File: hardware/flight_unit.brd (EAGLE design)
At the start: 160 x 100 mm, 25 parts, among them IC2 7805T, J1 DCJ0202, J2 CONN_20X2SHROUDED, T1 THERMISTOR-2,5, U1 4MB Flash, U2 4MB Flash, U3 4MB Flash

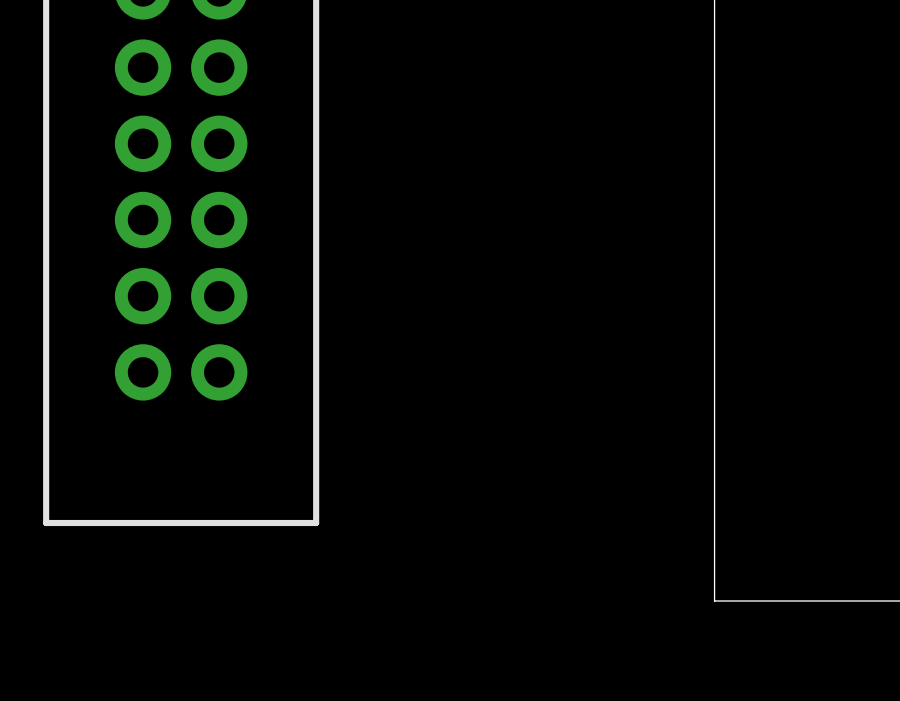
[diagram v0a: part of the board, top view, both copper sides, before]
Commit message: updated i/o headers
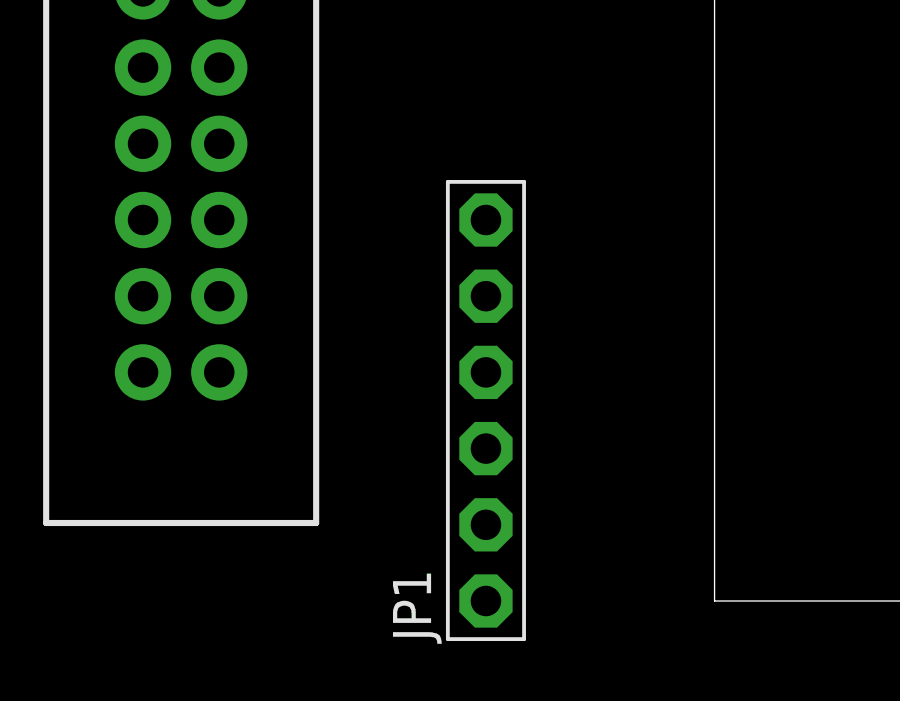
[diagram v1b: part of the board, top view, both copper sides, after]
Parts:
- added JP1: (no value), adafruit:1X06-BIG
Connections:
- removed net D_0: U$1.0/RX
- removed net D_1: U$1.1/TX
- removed net D_2: U$1.2
- removed net D_3: U$1.3/CANTX
- removed net D_4: U$1.4/CANRX
- new net SC_D0: J2.8, U$1.0/RX
- new net SC_D1: J2.12, U$1.1/TX
- new net SC_D2: J2.16, U$1.2
- new net SC_D3: J2.22, U$1.3/CANTX
- new net SC_D4: J2.36, U$1.4/CANRX
- net +3V3: now also U$3.VIN
- net GND: now also JP1.5, JP1.6, U$3.GND
- net IIC_SCL: now also J2.29, U$3.SCL
- net IIC_SDA: now also J2.7, U$3.SDA
- net SC_A0: now also JP1.1
- net SC_A1: now also JP1.2
- net SC_A2: now also JP1.3
- net SC_A3: now also JP1.4
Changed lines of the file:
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@@
 </element>
 <element name="U$3" library="adafruit" package="BNO055_BREAKOUT" value="IMU_BREAKOUT" x="10.16" y="64.77" smashed="yes"/>
+<element name="JP1" library="adafruit" package="1X06-BIG" value="" x="-7.62" y="6.35" smashed="yes" rot="R90">
+<attribute name="NAME" x="-9.4488" y="-1.3462" size="1.27" layer="25" ratio="10" rot="R90"/>
+<attribute name="VALUE" x="-4.445" y="-1.27" size="1.27" layer="27" rot="R90"/>
+</element>
 </elements>
 <signals>
@@
 <contactref element="T1" pad="1"/>
 <contactref element="R8" pad="1"/>
+<contactref element="U$3" pad="VIN"/>
 <wire x1="-20.19" y1="104.14" x2="-13.84" y2="104.14" width="0" layer="19" extent="1-1"/>
 <wire x1="-26.54" y1="104.14" x2="-20.19" y2="104.14" width="0" layer="19" extent="1-1"/>
@@
 <wire x1="-74.295" y1="106.94" x2="-68.58" y2="110.49" width="0" layer="19" extent="1-1"/>
 <wire x1="-48.26" y1="80.01" x2="-56.515" y2="106.94" width="0" layer="19" extent="1-1"/>
+<wire x1="17.145" y1="66.04" x2="-13.84" y2="104.14" width="0" layer="19" extent="1-1"/>
 <wire x1="-57.15" y1="2.54" x2="-48.26" y2="80.01" width="0" layer="19" extent="1-1"/>
 </signal>
@@
 <contactref element="RN2" pad="7"/>
 <contactref element="RN2" pad="5"/>
+<contactref element="U$3" pad="GND"/>
+<contactref element="JP1" pad="6"/>
+<contactref element="JP1" pad="5"/>
 <wire x1="-41.91" y1="118.11" x2="-31.75" y2="118.11" width="0" layer="19" extent="1-1"/>
 <wire x1="-52.07" y1="118.11" x2="-41.91" y2="118.11" width="0" layer="19" extent="1-1"/>
@@
 <wire x1="-16.51" y1="15.24" x2="-16.51" y2="20.32" width="0" layer="19" extent="1-1"/>
 <wire x1="-19.05" y1="7.62" x2="-16.51" y2="15.24" width="0" layer="19" extent="1-1"/>
+<wire x1="-7.62" y1="12.7" x2="-16.51" y2="15.24" width="0" layer="19" extent="1-1"/>
+<wire x1="-7.62" y1="10.16" x2="-7.62" y2="12.7" width="0" layer="19" extent="1-1"/>
 <wire x1="-34.415" y1="7.62" x2="-19.05" y2="7.62" width="0" layer="19" extent="1-1"/>
 <wire x1="-34.415" y1="5.08" x2="-34.415" y2="7.62" width="0" layer="19" extent="1-1"/>
@@
 <wire x1="-48.385" y1="10.16" x2="-48.385" y2="5.08" width="0" layer="19" extent="1-1"/>
 <wire x1="-59.69" y1="2.54" x2="-48.385" y2="5.08" width="0" layer="19" extent="1-1"/>
+<wire x1="22.225" y1="66.04" x2="-16.51" y2="50.8" width="0" layer="19" extent="1-1"/>
 </signal>
 <signal name="SC_5V0">
@@
 <signal name="IIC_SDA">
 <contactref element="U$1" pad="18/A4/SDA"/>
+<contactref element="U$3" pad="SDA"/>
+<contactref element="J2" pad="7"/>
+<wire x1="-19.05" y1="48.26" x2="24.765" y2="66.04" width="0" layer="19" extent="1-1"/>
+<wire x1="-27.94" y1="80.01" x2="-19.05" y2="48.26" width="0" layer="19" extent="1-1"/>
 </signal>
 <signal name="IIC_SCL">
 <contactref element="U$1" pad="19/A5/SCL"/>
-</signal>
-<signal name="D_0">
-<contactref element="U$1" pad="0/RX"/>
-</signal>
-<signal name="D_1">
-<contactref element="U$1" pad="1/TX"/>
-</signal>
-<signal name="D_2">
-<contactref element="U$1" pad="2"/>
-</signal>
-<signal name="D_3">
-<contactref element="U$1" pad="3/CANTX"/>
-</signal>
-<signal name="D_4">
-<contactref element="U$1" pad="4/CANRX"/>
+<contactref element="U$3" pad="SCL"/>
+<contactref element="J2" pad="29"/>
+<wire x1="-30.48" y1="80.01" x2="27.305" y2="66.04" width="0" layer="19" extent="1-1"/>
+<wire x1="-19.05" y1="20.32" x2="-30.48" y2="80.01" width="0" layer="19" extent="1-1"/>
 </signal>
 <signal name="LED_0">
@@
 <signal name="SC_A3">
 <contactref element="RN2" pad="13"/>
+<contactref element="JP1" pad="4"/>
+<wire x1="-7.62" y1="7.62" x2="-40.515" y2="12.7" width="0" layer="19" extent="1-1"/>
 </signal>
 <signal name="SC_A2">
 <contactref element="RN2" pad="14"/>
+<contactref element="JP1" pad="3"/>
+<wire x1="-7.62" y1="5.08" x2="-40.515" y2="15.24" width="0" layer="19" extent="1-1"/>
 </signal>
 <signal name="SC_A1">
 <contactref element="RN2" pad="15"/>
+<contactref element="JP1" pad="2"/>
+<wire x1="-7.62" y1="2.54" x2="-40.515" y2="17.78" width="0" layer="19" extent="1-1"/>
 </signal>
 <signal name="SC_A0">
 <contactref element="RN2" pad="16"/>
+<contactref element="JP1" pad="1"/>
+<wire x1="-7.62" y1="0" x2="-40.515" y2="20.32" width="0" layer="19" extent="1-1"/>
+</signal>
+<signal name="SC_D0">
+<contactref element="J2" pad="8"/>
+<contactref element="U$1" pad="0/RX"/>
+<wire x1="-45.72" y1="64.77" x2="-16.51" y2="48.26" width="0" layer="19" extent="1-1"/>
+</signal>
+<signal name="SC_D1">
+<contactref element="J2" pad="12"/>
+<contactref element="U$1" pad="1/TX"/>
+<wire x1="-43.18" y1="64.77" x2="-16.51" y2="43.18" width="0" layer="19" extent="1-1"/>
+</signal>
+<signal name="SC_D2">
+<contactref element="J2" pad="16"/>
+<contactref element="U$1" pad="2"/>
+<wire x1="-40.64" y1="64.77" x2="-16.51" y2="38.1" width="0" layer="19" extent="1-1"/>
+</signal>
+<signal name="SC_D3">
+<contactref element="J2" pad="22"/>
+<contactref element="U$1" pad="3/CANTX"/>
+<wire x1="-16.51" y1="30.48" x2="-38.1" y2="64.77" width="0" layer="19" extent="1-1"/>
+</signal>
+<signal name="SC_D4">
+<contactref element="J2" pad="36"/>
+<contactref element="U$1" pad="4/CANRX"/>
+<wire x1="-16.51" y1="12.7" x2="-35.56" y2="64.77" width="0" layer="19" extent="1-1"/>
 </signal>
 </signals>

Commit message: added start of fram framework
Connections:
- net MEM_CS0: now also U$1.8; no longer U$1.10/CS
- net MEM_CS2: now also U$1.10/CS; no longer U$1.8
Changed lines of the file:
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@@
 </signal>
 <signal name="MEM_CS0">
-<contactref element="U$1" pad="10/CS"/>
 <contactref element="U1" pad="1"/>
-<wire x1="-56.515" y1="101.34" x2="-20.32" y2="64.77" width="0" layer="19" extent="1-1"/>
+<contactref element="U$1" pad="8"/>
+<wire x1="-25.4" y1="64.77" x2="-56.515" y2="101.34" width="0" layer="19" extent="1-1"/>
 </signal>
 <signal name="MEM_CS1">
@@
 </signal>
 <signal name="MEM_CS2">
-<contactref element="U$1" pad="8"/>
 <contactref element="U3" pad="1"/>
-<wire x1="-74.295" y1="101.34" x2="-25.4" y2="64.77" width="0" layer="19" extent="1-1"/>
+<contactref element="U$1" pad="10/CS"/>
+<wire x1="-74.295" y1="101.34" x2="-20.32" y2="64.77" width="0" layer="19" extent="1-1"/>
 </signal>
 <signal name="IIC_SDA">

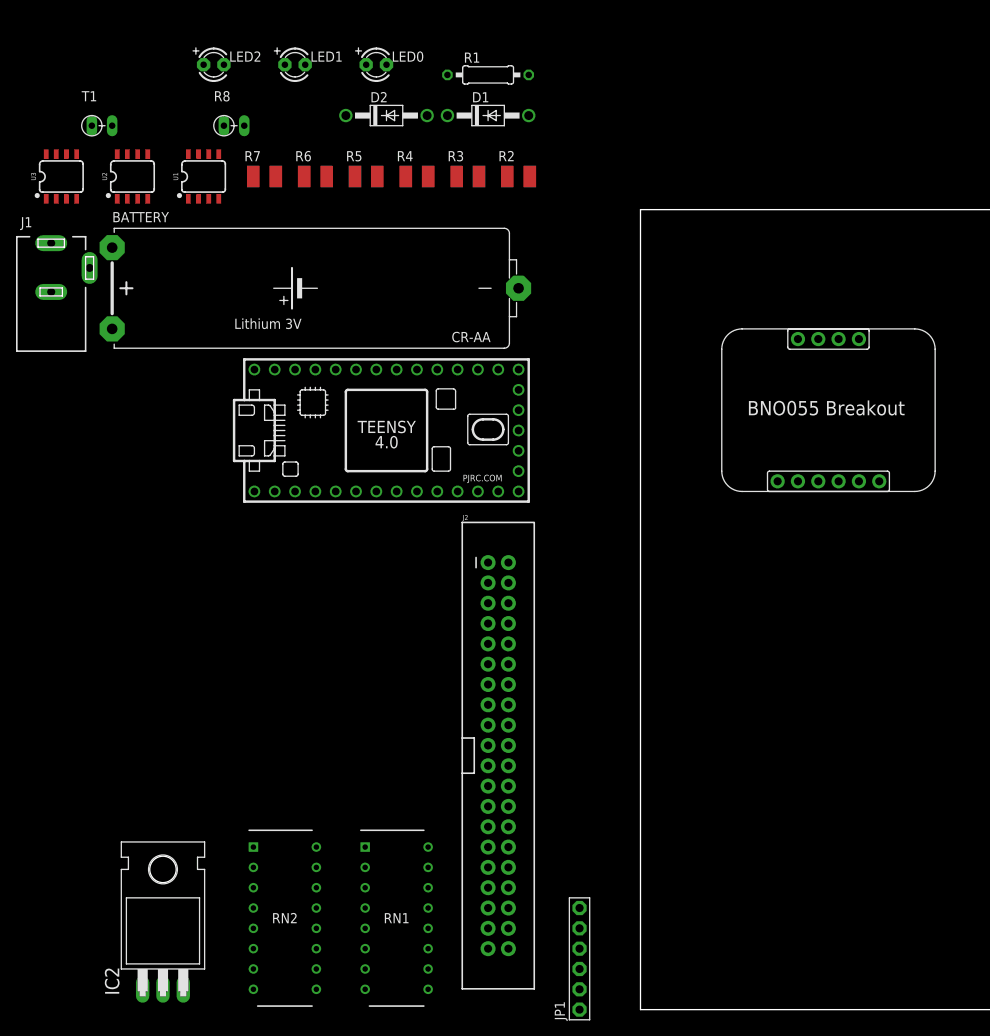
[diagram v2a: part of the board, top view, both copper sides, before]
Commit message: fix back annotation error
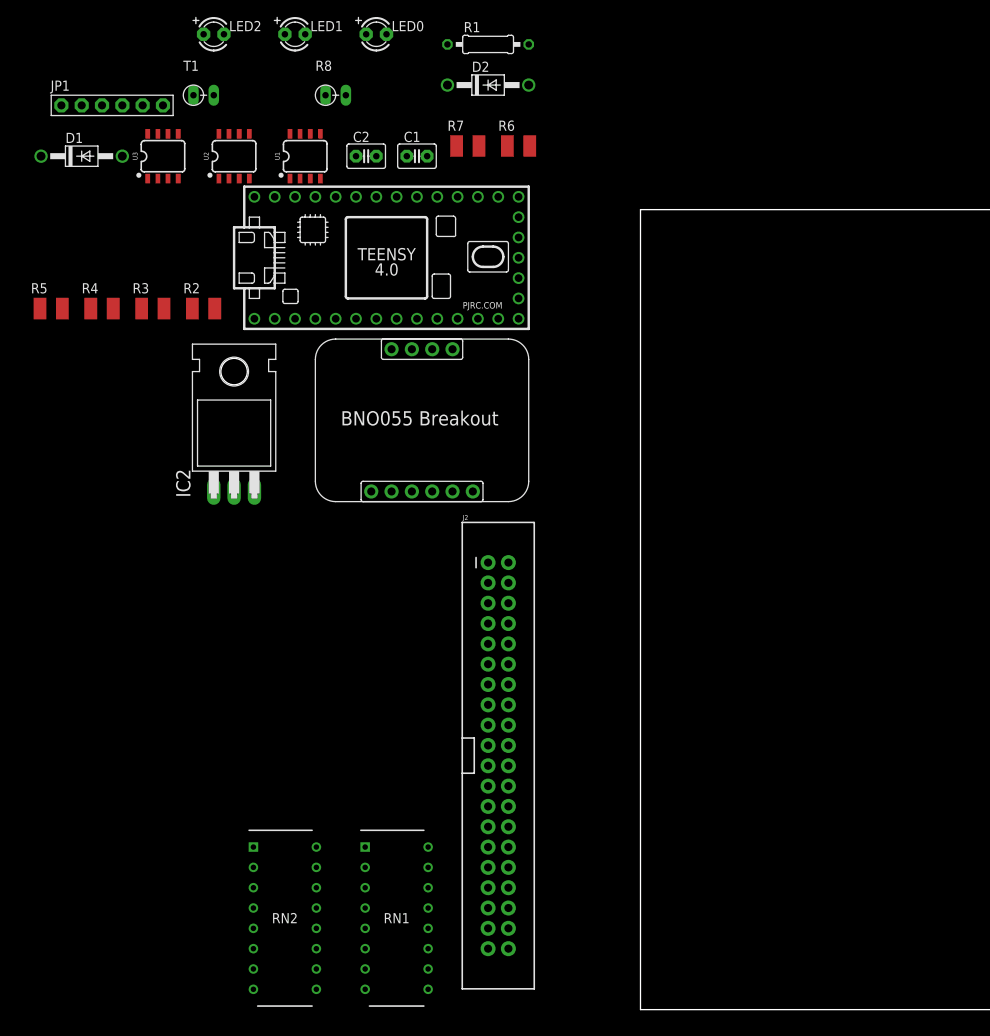
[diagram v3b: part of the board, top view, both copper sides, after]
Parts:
- removed BATTERY: 5V, battery:CRAA
- removed J1: DCJ0202, con-jack:DCJ0202
- added C1, C2: 0.1uf, capacitor-wima:C2.5-3
- R1: value 1k -> 3.3k
- moved JP1 121.6 mm to (-66.0, 113.0), turned to 0 degrees
- moved IC2 62.9 mm to (-50.8, 74.9)
- moved D1 51.1 mm to (-69.8, 106.7)
- moved U$3 50.8 mm to (-40.6, 63.5)
- moved R3 42.7 mm to (-61.0, 87.6)
- moved R4 42.7 mm to (-67.3, 87.6)
- moved R2 42.7 mm to (-54.6, 87.6)
- moved R5 42.7 mm to (-73.7, 87.6)
- moved R7 25.7 mm to (-21.6, 108.0)
- moved R6 25.7 mm to (-15.2, 108.0)
- moved U$1 21.6 mm to (-31.8, 94.0)
- moved T1 13.3 mm to (-54.6, 114.3)
- moved D2 13.3 mm to (-19.1, 115.6)
- moved R8 13.3 mm to (-38.1, 114.3)
- moved U1 13.0 mm to (-41.9, 106.7)
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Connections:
- net +3V3: now also C1.1
- net GND: now also C1.2, C2.2; no longer BATTERY.-, J1.2
- net N$1: no longer BATTERY.+
- net N$2: now also C2.1
- net N$4: no longer J1.1

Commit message: Add files via upload
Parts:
- removed C1, C2: 0.1uf, capacitor-wima:C2.5-3
- added E$1, E$2: (no value), con-jst:B4B-ZR
- added E$3, E$4: (no value), rcl:B45181A
- R1: value 3.3k -> 1k
- moved JP1 121.6 mm to (-7.62, 6.35), turned to 90 degrees
- moved IC2 62.9 mm to (-59.7, 12.7)
- moved D1 51.6 mm to (-19.1, 97.8)
- moved U$3 50.8 mm to (10.2, 64.8)
- moved R3 39.5 mm to (-21.6, 90.2)
- moved R4 39.5 mm to (-27.9, 90.2)
- moved R2 39.5 mm to (-15.2, 90.2)
- moved R5 39.5 mm to (-34.3, 90.2)
- moved R7 31.0 mm to (-47.0, 90.2)
- moved R6 31.0 mm to (-40.6, 90.2)
- moved T1 21.8 mm to (-67.3, 96.5)
- moved R8 21.8 mm to (-50.8, 96.5)
- moved D2 21.8 mm to (-31.8, 97.8)
- moved U$1 21.6 mm to (-31.8, 72.4)
- moved U1 20.8 mm to (-54.6, 90.2)
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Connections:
- net +3V3: now also E$4.+; no longer C1.1
- net GND: now also E$1.1, E$2.1, E$3.-, E$4.-; no longer C1.2, C2.2
- net N$1: now also E$1.2
- net N$2: now also E$3.+; no longer C2.1
- net N$4: now also E$2.2
